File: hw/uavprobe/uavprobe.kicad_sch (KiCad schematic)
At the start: 0 parts

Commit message: RP2040 sheet
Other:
- added sheet CAN (can.kicad_sch)
- added sheet Connectors (connectors.kicad_sch)
- added sheet RP2040 (rp2040.kicad_sch)
- added sheet USB (usb.kicad_sch)
- title: (none) -> UAV Sensor Probe
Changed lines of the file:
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@@
 	(generator_version "9.0")
 	(paper "A4")
+	(title_block
+		(title "UAV Sensor Probe")
+		(date "2025-08-24")
+		(rev "1")
+		(comment 1 "Oleksiy Protas")
+	)
+	(sheet
+		(at 195.58 66.04)
+		(size 44.45 44.45)
+		(exclude_from_sim no)
+		(in_bom yes)
+		(on_board yes)
+		(dnp no)
+		(fields_autoplaced yes)
+		(stroke
+			(width 0.1524)
+			(type solid)
+		)
+		(fill
+			(color 0 0 0 0.0000)
+		)
+		(property "Sheetname" "CAN"
+			(at 195.58 65.3284 0)
+			(effects
+				(font
+					(size 1.27 1.27)
+				)
+				(justify left bottom)
+			)
+		)
+		(property "Sheetfile" "can.kicad_sch"
+			(at 195.58 111.0746 0)
+			(effects
+				(font
+					(size 1.27 1.27)
+				)
+				(justify left top)
+			)
+		)
+		(instances
+			(project "uavprobe"
+				(path "/e4efab0a-eb38-47b4-a7c8-7fdbedea4819"
+					(page "5")
+				)
+			)
+		)
+	)
+	(sheet
+		(at 139.7 57.15)
+		(size 29.21 40.64)
+		(exclude_from_sim no)
+		(in_bom yes)
+		(on_board yes)
+		(dnp no)
+		(fields_autoplaced yes)
+		(stroke
+			(width 0.1524)
+			(type solid)
+		)
+		(fill
+			(color 0 0 0 0.0000)
+		)
+		(property "Sheetname" "USB"
+			(at 139.7 56.4384 0)
+			(effects
+				(font
+					(size 1.27 1.27)
+				)
+				(justify left bottom)
+			)
+		)
+		(property "Sheetfile" "usb.kicad_sch"
+			(at 139.7 98.3746 0)
+			(effects
+				(font
+					(size 1.27 1.27)
+				)
+				(justify left top)
+			)
+		)
+		(instances
+			(project "uavprobe"
+				(path "/e4efab0a-eb38-47b4-a7c8-7fdbedea4819"
+					(page "3")
+				)
+			)
+		)
+	)
+	(sheet
+		(at 29.21 71.12)
+		(size 53.34 41.91)
+		(exclude_from_sim no)
+		(in_bom yes)
+		(on_board yes)
+		(dnp no)
+		(fields_autoplaced yes)
+		(stroke
+			(width 0.1524)
+			(type solid)
+		)
+		(fill
+			(color 0 0 0 0.0000)
+		)
+		(property "Sheetname" "RP2040"
+			(at 29.21 70.4084 0)
+			(effects
+				(font
+					(size 1.27 1.27)
+				)
+				(justify left bottom)
+			)
+		)
+		(property "Sheetfile" "rp2040.kicad_sch"
+			(at 29.21 113.6146 0)
+			(effects
+				(font
+					(size 1.27 1.27)
+				)
+				(justify left top)
+			)
+		)
+		(instances
+			(project "uavprobe"
+				(path "/e4efab0a-eb38-47b4-a7c8-7fdbedea4819"
+					(page "2")
+				)
+			)
+		)
+	)
+	(sheet
+		(at 123.19 119.38)
+		(size 44.45 26.67)
+		(exclude_from_sim no)
+		(in_bom yes)
+		(on_board yes)
+		(dnp no)
+		(fields_autoplaced yes)
+		(stroke
+			(width 0.1524)
+			(type solid)
+		)
+		(fill
+			(color 0 0 0 0.0000)
+		)
+		(property "Sheetname" "Connectors"
+			(at 123.19 118.6684 0)
+			(effects
+				(font
+					(size 1.27 1.27)
+				)
+				(justify left bottom)
+			)
+		)
+		(property "Sheetfile" "connectors.kicad_sch"
+			(at 123.19 146.6346 0)
+			(effects
+				(font
+					(size 1.27 1.27)
+				)
+				(justify left top)
+			)
+		)
+		(instances
+			(project "uavprobe"
+				(path "/e4efab0a-eb38-47b4-a7c8-7fdbedea4819"
+					(page "4")
+				)
+			)
+		)
+	)
 	(sheet_instances
 		(path "/"

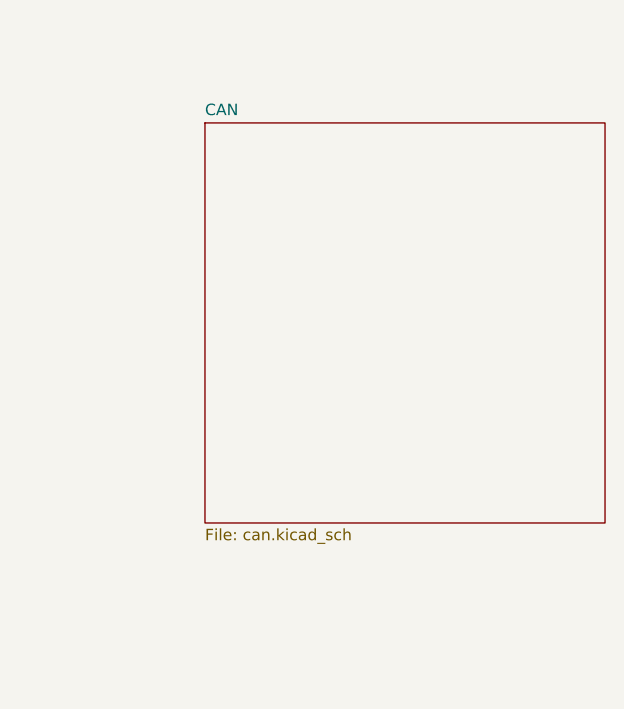
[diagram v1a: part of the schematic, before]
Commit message: Connectors sheet and CAN/ESD
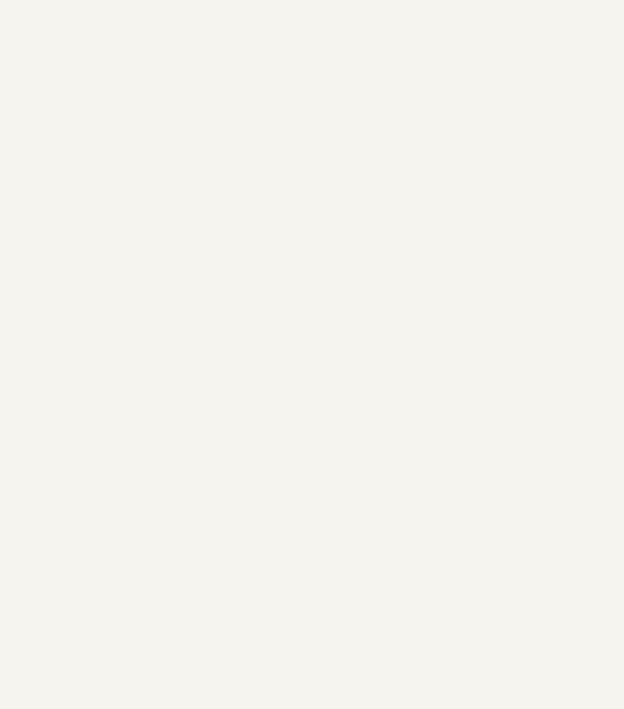
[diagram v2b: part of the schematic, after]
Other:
- removed sheet CAN
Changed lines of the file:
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@@
-	)
-	(sheet
-		(at 195.58 66.04)
-		(size 44.45 44.45)
-		(exclude_from_sim no)
-		(in_bom yes)
-		(on_board yes)
-		(dnp no)
-		(fields_autoplaced yes)
-		(stroke
-			(width 0.1524)
-			(type solid)
-		)
-		(fill
-			(color 0 0 0 0.0000)
-		)
-		(property "Sheetname" "CAN"
-			(at 195.58 65.3284 0)
-			(effects
-				(font
-					(size 1.27 1.27)
-				)
-				(justify left bottom)
-			)
-		)
-		(property "Sheetfile" "can.kicad_sch"
-			(at 195.58 111.0746 0)
-			(effects
-				(font
-					(size 1.27 1.27)
-				)
-				(justify left top)
-			)
-		)
-		(instances
-			(project "uavprobe"
-				(path "/e4efab0a-eb38-47b4-a7c8-7fdbedea4819"
-					(page "5")
-				)
-			)
-		)
 	)
 	(sheet

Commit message: Cleanup and root sheet
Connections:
- no-connect marks 0 -> 2
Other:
- sheet Connectors ports: added CAN1_D+, CAN1_D-, CAN2_D+, CAN2_D-, I2C_SCL, I2C_SDA, UART1_CTS, UART1_RTS, UART1_RX, UART1_TX, UART2_RX, UART2_TX, USB2_D+, USB2_D-, VBUS, VBUS2; removed none
- sheet RP2040 ports: added CAN1_D+, CAN1_D-, CAN2_D+, CAN2_D-, I2C_SCL, I2C_SDA, UART1_RX, UART1_TX, UART2_RX, UART2_TX, USB1_D+, USB1_D-, VBUS1; removed none
- sheet USB ports: added USB1_D+, USB1_D-, USB2_D+, USB2_D-, VBUS, VBUS1, VBUS2; removed none
- note added: "NB: Flow control pins unconnected!"

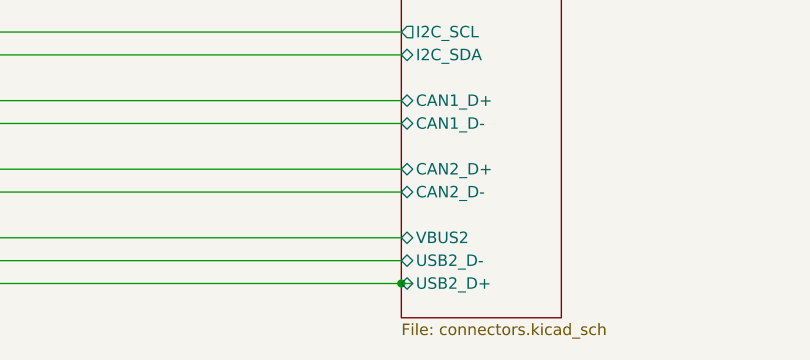
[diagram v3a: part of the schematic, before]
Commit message: ERC pass
Footprint and symbol copy editing warnings left
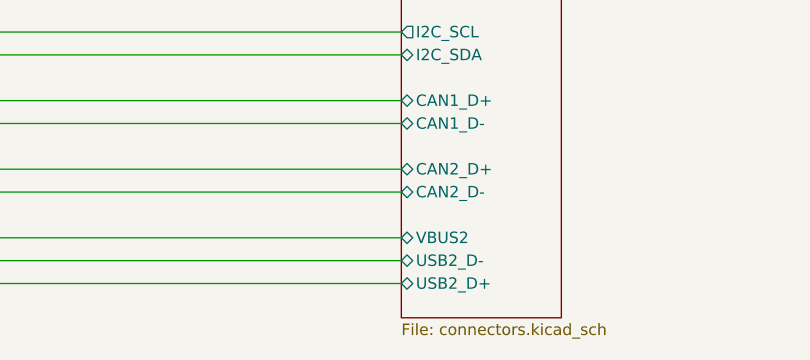
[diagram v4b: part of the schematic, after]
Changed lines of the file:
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@@
 		)
-	)
-	(junction
-		(at 224.79 107.95)
-		(diameter 0)
-		(color 0 0 0 0)
 	)
 	(no_connect
@@
 		)
 		(stroke
-			(width 0)
-			(type default)
-		)
-	)
-	(wire
-		(pts
-			(xy 226.06 107.95) (xy 224.79 107.95)
-		)
-		(stroke
